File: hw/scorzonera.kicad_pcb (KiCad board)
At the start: 2 copper layers, 70.7 x 53.3 mm, 16 parts, among them J1 NEIGHBOR1, J2 NEIGHBOR2, J3 Conn_01x02, J4 Conn_01x02, J7 BONUS_ROW, U1 AM7969, U2 74ALVC164245, U3 MAX3232

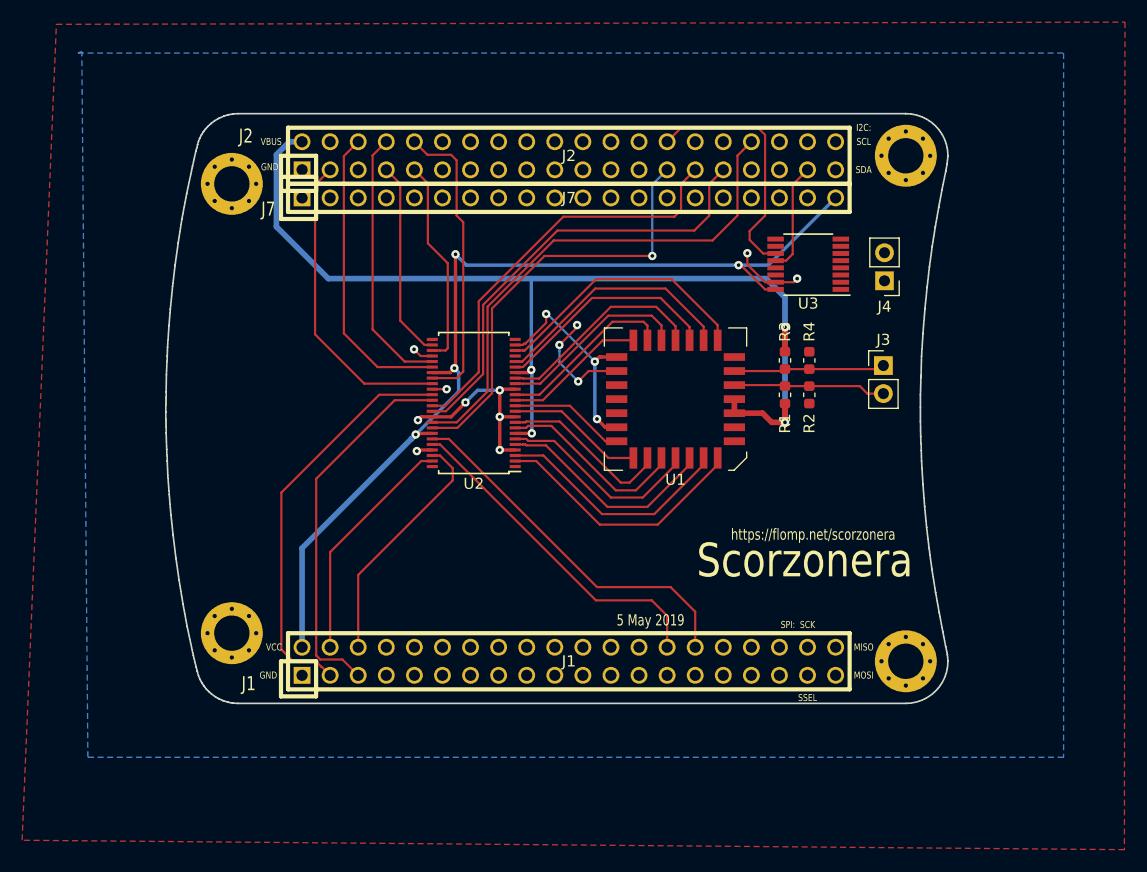
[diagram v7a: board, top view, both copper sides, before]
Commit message: Add Wago connector, more routing
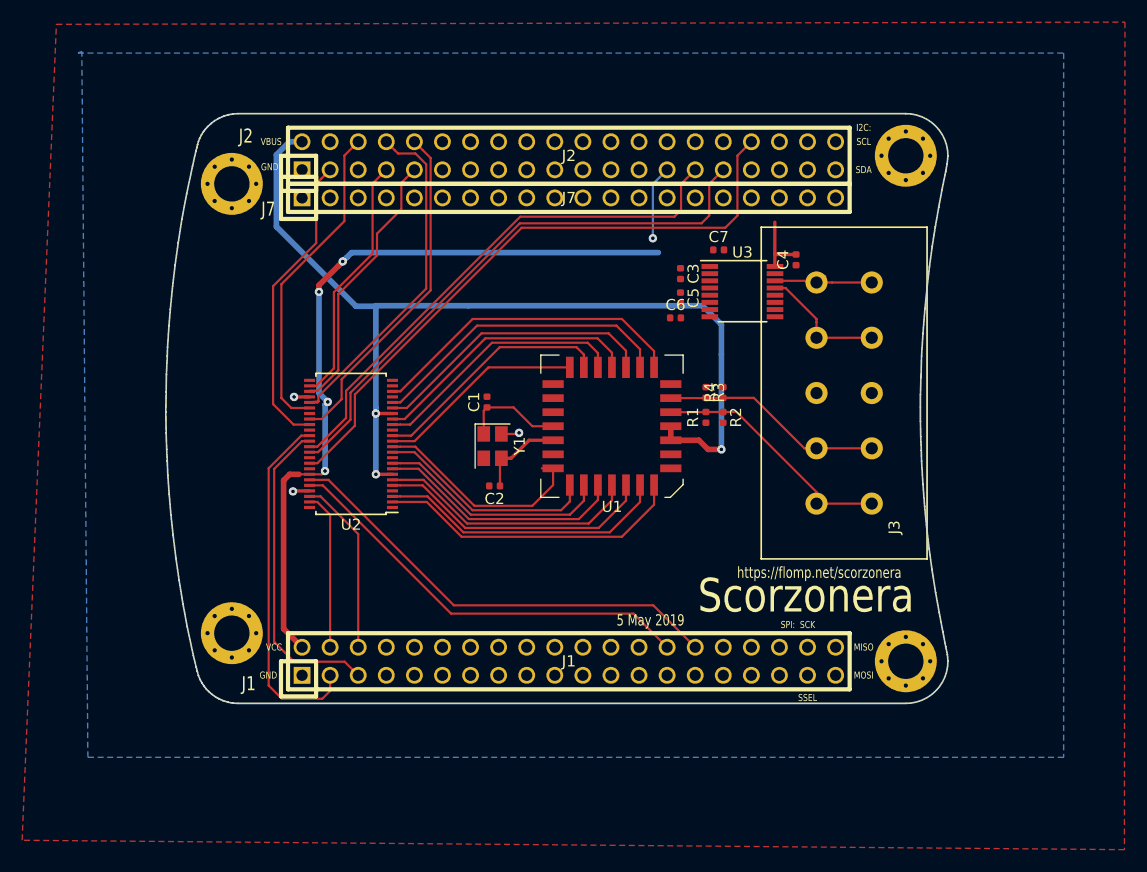
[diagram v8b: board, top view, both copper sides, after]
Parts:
- removed J4: Conn_01x02, Connector_PinHeader_2.54mm:PinHeader_1x02_P2.54mm_Vertical
- added C1: C, Capacitor_SMD:C_0402_1005Metric, F.Cu at (138.7, 94.7)
- added C2: C, Capacitor_SMD:C_0402_1005Metric, F.Cu at (139.3, 102.2)
- added C3: 100n, Capacitor_SMD:C_0402_1005Metric, F.Cu at (156.2, 83.0)
- added C4: 100n, Capacitor_SMD:C_0402_1005Metric, F.Cu at (166.6, 81.8)
- added C5: 100n, Capacitor_SMD:C_0402_1005Metric, F.Cu at (156.2, 85.2)
- added C6: 100n, Capacitor_SMD:C_0402_1005Metric, F.Cu at (155.7, 87.0)
- added C7: 100n, Capacitor_SMD:C_0402_1005Metric, F.Cu at (159.6, 80.9)
- added Y1: Crystal_GND24, Crystal:Crystal_SMD_SeikoEpson_TSX3225-4Pin_3.2x2.5mm, F.Cu at (139.2, 98.7)
- J3: value Conn_01x02 -> Conn_01x05; footprint Connector_PinHeader_2.54mm:PinHeader_1x02_P2.54mm_Vertical -> wago:256-743-5
- R1, R2, R3, R4: footprint Resistor_SMD:R_0603_1608Metric -> Resistor_SMD:R_0402_1005Metric
- moved U2 11.7 mm to (126.3, 98.5)
- moved R4 8.32 mm to (160.0, 93.8)
- moved R2 8.06 mm to (160.0, 96.0)
- moved R3 7.72 mm to (158.4, 93.8)
- moved R1 7.43 mm to (158.4, 96.0)
- moved U3 6.44 mm to (161.8, 84.7), turned to 0 degrees
- moved U1 6.25 mm to (149.9, 96.8)
- moved J3 2.70 mm to (173.4, 93.8), turned to 90 degrees
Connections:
- J3 pad 1: /SERIN- -> /SERIN+
- J3 pad 2: /SERIN+ -> /SERIN-
- U1 pad 22: Net-(U1-Pad22) -> /X1
- U1 pad 23: Net-(U1-Pad23) -> /X2
- U3 pad 13: Net-(J4-Pad2) -> /RS232_RX
- U3 pad 14: Net-(J4-Pad1) -> /RS232_TX
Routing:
- net GND: track 39.5 -> 4.56 mm, vias 13 -> 3
- net /SGPIO4: track 39.2 -> 6.72 mm
- net /U1_TXD: track 22.6 -> 0.00 mm
- net /CLK: track 20.1 -> 0.00 mm, vias 3 -> 0
- net VCC: track 86.9 -> 75.0 mm
- net /RS232_RX: track 0.00 -> 11.6 mm
- net /SGPIO6: track 40.7 -> 51.1 mm
- net /SGPIO7: track 37.8 -> 48.1 mm
- net /U1_RXD: track 9.97 -> 0.00 mm
- net /SGPIO5: track 47.0 -> 56.8 mm
- net /DO7: track 10.5 -> 20.1 mm
- net /RS232_TX: track 0.00 -> 9.38 mm
- net /X1: track 0.00 -> 9.21 mm
- net /SERIN+: track 13.8 -> 22.2 mm
- net /X2: track 0.00 -> 7.91 mm
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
